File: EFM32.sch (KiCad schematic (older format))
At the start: 9 parts, among them J5 MCU_debug, J6 67997-410HLF, U7 EFM32GG11B4xx, Y1 48Mhz

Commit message: Added in the potentiometers, fixed some faulty pins on the artix, rewired some pins on the MCU so they didn't interfere with the crystal.
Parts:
- RV1, RV2: footprint (none) -> Potentiometer_SMD:Potentiometer_Bourns_PRS11S_Vertical
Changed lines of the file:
@@
 F 0 "RV2" H 8180 2404 50  0000 R CNN
 F 1 "R_POT" H 8180 2495 50  0000 R CNN
-F 2 "" H 8250 2450 50  0001 C CNN
+F 2 "Potentiometer_SMD:Potentiometer_Bourns_PRS11S_Vertical" H 8250 2450 50  0001 C CNN
 F 3 "~" H 8250 2450 50  0001 C CNN
 	1    8250 2450
@@
 F 0 "RV1" H 8180 1804 50  0000 R CNN
 F 1 "R_POT" H 8180 1895 50  0000 R CNN
-F 2 "" H 8250 1850 50  0001 C CNN
+F 2 "Potentiometer_SMD:Potentiometer_Bourns_PRS11S_Vertical" H 8250 1850 50  0001 C CNN
 F 3 "~" H 8250 1850 50  0001 C CNN
 	1    8250 1850

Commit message: Wired up the potentiometers.
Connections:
- wire segments 118 -> 121
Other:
- note removed: "why the PWR_FLAG?"
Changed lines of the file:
@@
 L power:+3.3VA #PWR?
 U 1 1 5D8A3009
-P 4100 4100
+P 4000 4050
 AR Path="/5D8A3009" Ref="#PWR?"  Part="1"
 AR Path="/5D8502F2/5D8A3009" Ref="#PWR034"  Part="1"
-F 0 "#PWR034" H 4100 3950 50  0001 C CNN
-F 1 "+3.3VA" H 3800 4100 50  0000 L CNN
-F 2 "" H 4100 4100 50  0001 C CNN
-F 3 "" H 4100 4100 50  0001 C CNN
-	1    4100 4100
+F 0 "#PWR034" H 4000 3900 50  0001 C CNN
+F 1 "+3.3VA" H 3700 4050 50  0000 L CNN
+F 2 "" H 4000 4050 50  0001 C CNN
+F 3 "" H 4000 4050 50  0001 C CNN
+	1    4000 4050
 	1    0    0    -1
 $EndComp
@@
 F 3 "" H 3850 4600 50  0001 C CNN
 	1    3850 4600
-	1    0    0    -1
-$EndComp
-$Comp
-L power:PWR_FLAG #FLG?
-U 1 1 5D8A301C
-P 5400 3900
-AR Path="/5D8A301C" Ref="#FLG?"  Part="1"
-AR Path="/5D8502F2/5D8A301C" Ref="#FLG01"  Part="1"
-F 0 "#FLG01" H 5400 3975 50  0001 C CNN
-F 1 "PWR_FLAG" H 5400 4073 50  0000 C CNN
-F 2 "" H 5400 3900 50  0001 C CNN
-F 3 "~" H 5400 3900 50  0001 C CNN
-	1    5400 3900
 	1    0    0    -1
 $EndComp
@@
 	0    -1   -1   0
 $EndComp
-Wire Wire Line
-	4100 4100 4100 4200
-Connection ~ 4100 4100
-Connection ~ 5400 3900
 Wire Wire Line
 	5400 4100 5400 4200
@@
 Wire Wire Line
 	4600 6700 4300 6700
-Text Notes 5000 3650 0    50   ~ 0
-why the PWR_FLAG?
 Wire Wire Line
 	6700 6600 6750 6600
@@
 NoConn ~ 8250 2600
 NoConn ~ 8250 1700
+Wire Wire Line
+	4100 4200 4000 4200
+Wire Wire Line
+	4000 4200 4000 4100
+Wire Wire Line
+	4100 4100 4000 4100
+Connection ~ 4000 4100
+Wire Wire Line
+	4000 4100 4000 4050
 $EndSCHEMATC

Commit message: Started wiring the flash chip.
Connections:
- wire segments 121 -> 122
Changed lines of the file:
@@
 L power:+3.3VA #PWR?
 U 1 1 5D907864
-P 3850 4950
+P 3850 4900
 AR Path="/5D907864" Ref="#PWR?"  Part="1"
 AR Path="/5D8502F2/5D907864" Ref="#PWR030"  Part="1"
-F 0 "#PWR030" H 3850 4800 50  0001 C CNN
-F 1 "+3.3VA" H 3750 4900 50  0000 L CNN
-F 2 "" H 3850 4950 50  0001 C CNN
-F 3 "" H 3850 4950 50  0001 C CNN
-	1    3850 4950
+F 0 "#PWR030" H 3850 4750 50  0001 C CNN
+F 1 "+3.3VA" H 3750 4850 50  0000 L CNN
+F 2 "" H 3850 4900 50  0001 C CNN
+F 3 "" H 3850 4900 50  0001 C CNN
+	1    3850 4900
 	1    0    0    -1
 $EndComp
@@
 Wire Wire Line
 	4000 4100 4000 4050
+Wire Wire Line
+	3850 4950 3850 4900
 $EndSCHEMATC

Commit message: Wire up 1V PSU. Use smaller footprints for small caps.
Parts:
- C6: footprint Capacitor_SMD:C_1206_3216Metric_Pad1.42x1.75mm_HandSolder -> Capacitor_SMD:C_0805_2012Metric_Pad1.15x1.40mm_HandSolder
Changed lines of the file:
@@
 F 0 "C6" V 5600 3950 50  0000 L CNN
 F 1 "1u" V 5600 3750 50  0000 L CNN
-F 2 "Capacitor_SMD:C_1206_3216Metric_Pad1.42x1.75mm_HandSolder" H 5688 3750 50  0001 C CNN
+F 2 "Capacitor_SMD:C_0805_2012Metric_Pad1.15x1.40mm_HandSolder" H 5688 3750 50  0001 C CNN
 F 3 "~" H 5650 3900 50  0001 C CNN
 	1    5650 3900

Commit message: Rearrange and wire most of PCB FOR REAL THIS TIME
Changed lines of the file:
@@
 Wire Wire Line
 	2300 3900 4100 3900
-Entry Wire Line
-	10100 6050 10200 6150
 Text HLabel 4300 6700 0    50   UnSpc ~ 0
 USB_D+

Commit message: Fix a few more noclipping objects and labels
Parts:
- J6: value 67997-410HLF -> MCU_GPIO
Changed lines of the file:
@@
 P 6750 6750
 F 0 "J6" H 7400 7237 60  0000 C CNN
-F 1 "67997-410HLF" H 7400 7131 60  0000 C CNN
+F 1 "MCU_GPIO" H 7400 7131 60  0000 C CNN
 F 2 "footprints:67997-410HLF" H 7400 7090 60  0001 C CNN
 F 3 "" H 6750 6900 60  0000 C CNN

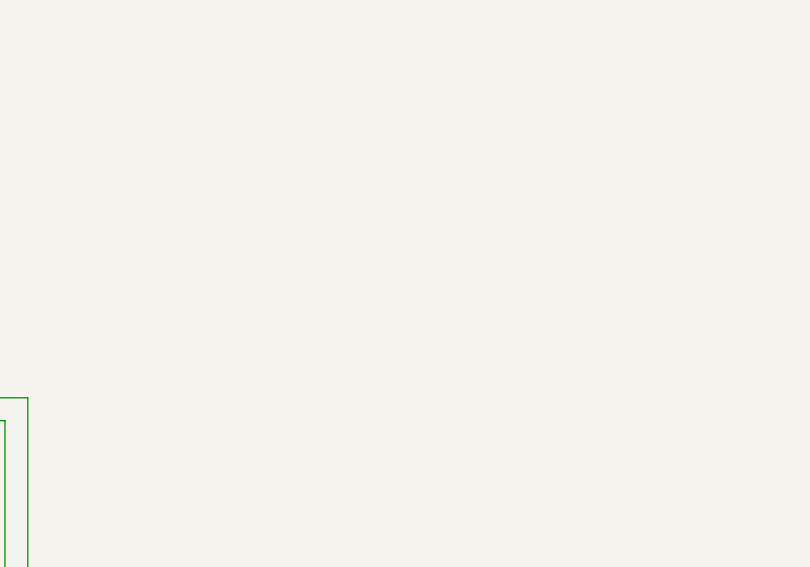
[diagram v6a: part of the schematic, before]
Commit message: Removed pull-down resistors.
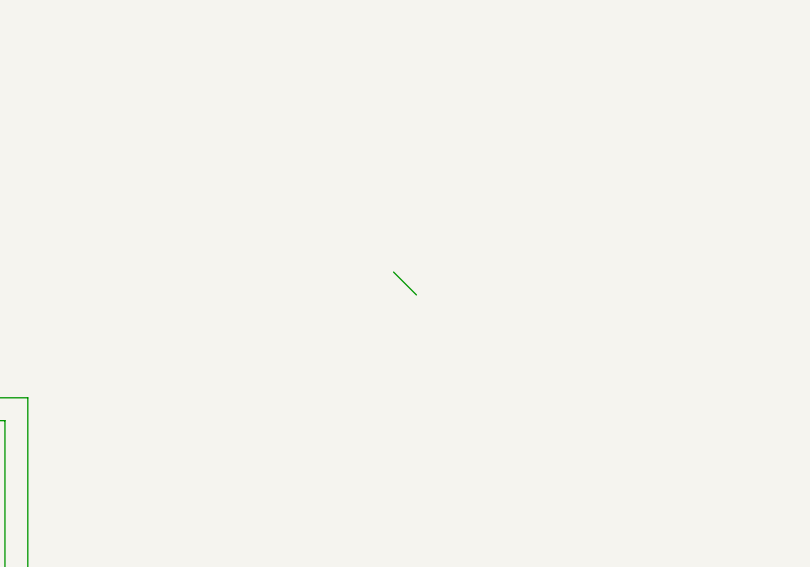
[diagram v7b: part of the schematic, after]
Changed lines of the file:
@@
 Wire Wire Line
 	2300 3900 4100 3900
+Entry Wire Line
+	10100 6050 10200 6150
 Text HLabel 4300 6700 0    50   UnSpc ~ 0
 USB_D+
